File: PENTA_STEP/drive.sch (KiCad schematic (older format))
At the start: 17 parts, among them U3 TMC5160-TA

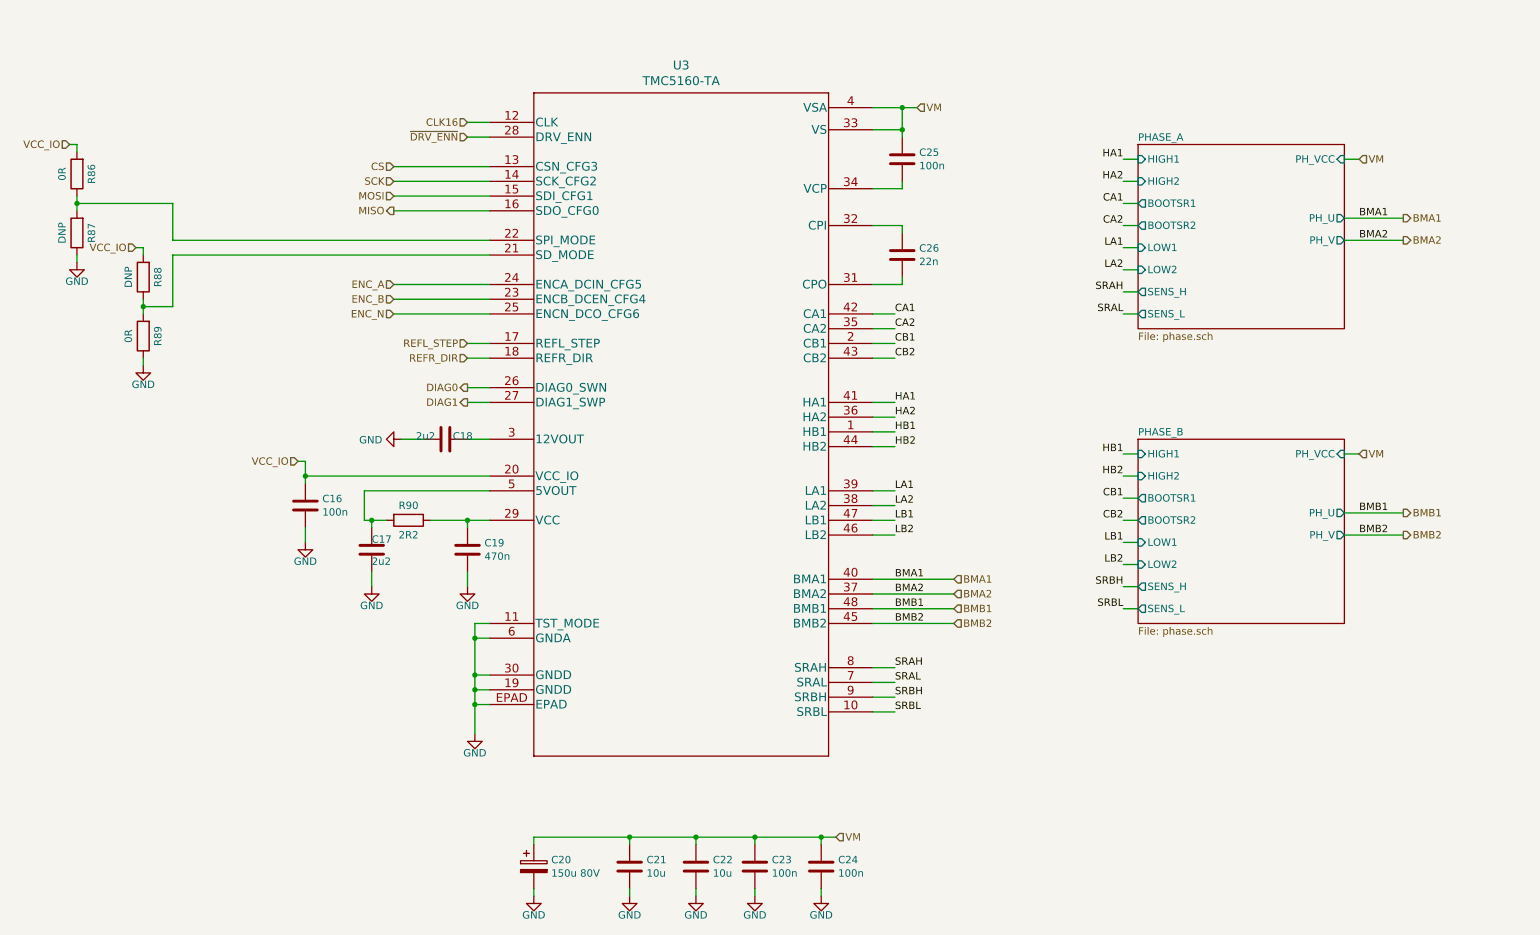
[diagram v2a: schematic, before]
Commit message: Added two FET-controlled outputs to the board
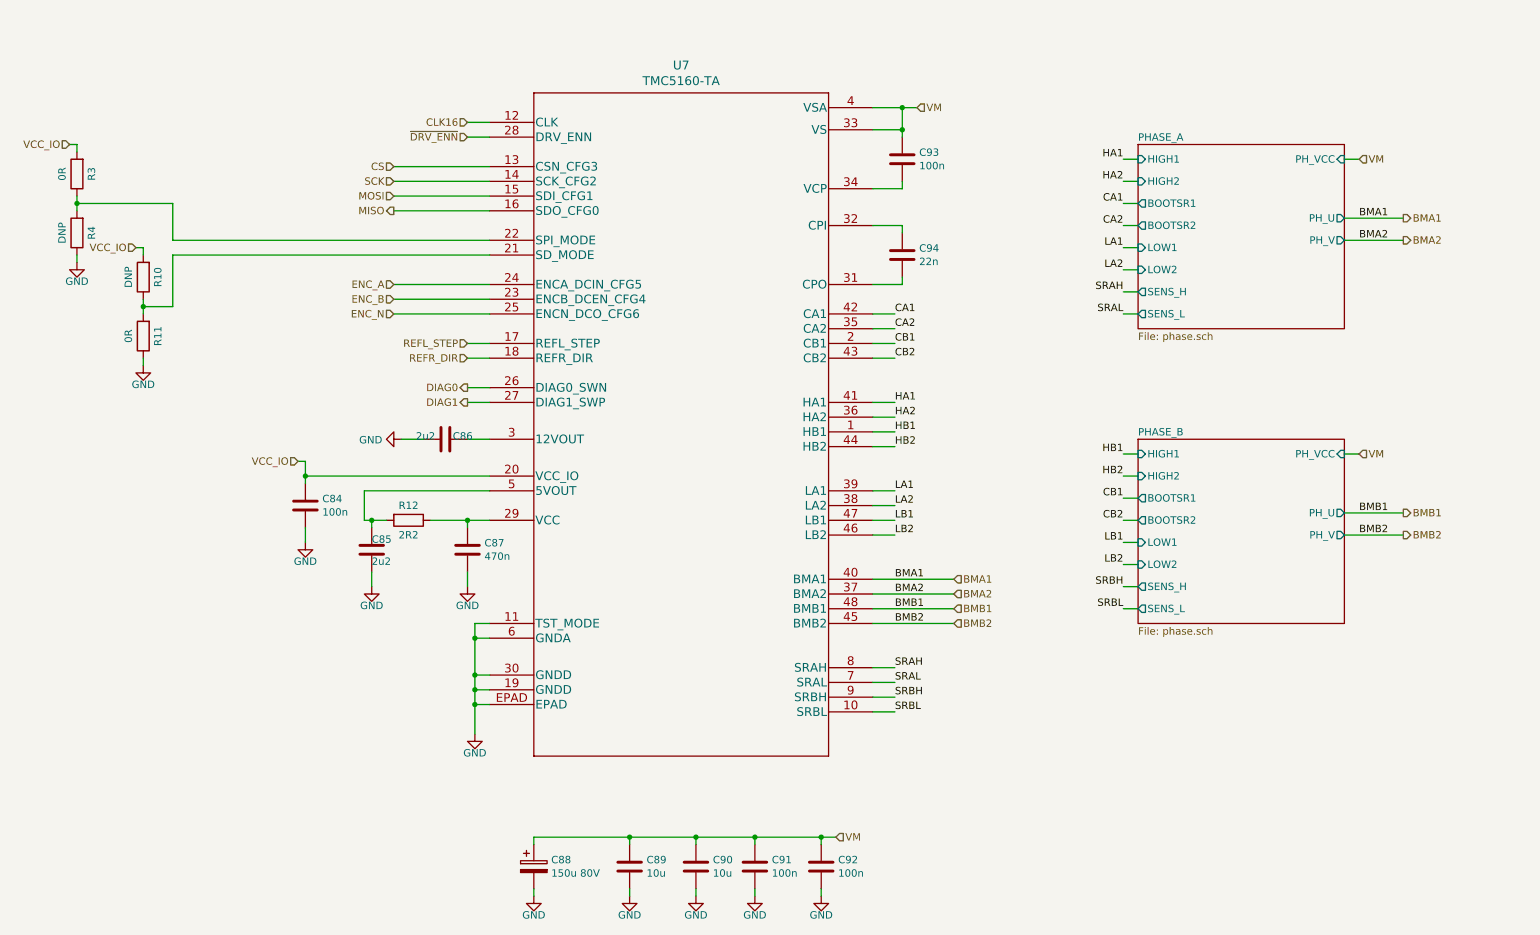
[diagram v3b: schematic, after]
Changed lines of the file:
@@
 $Descr A4 11693 8268
 encoding utf-8
-Sheet 2 16
+Sheet 14 16
 Title ""
 Date ""
@@
 AR Path="/5E50B60F/5E4B8E3D" Ref="U6"  Part="1"
 AR Path="/5F24B60D/5E4B8E3D" Ref="U7"  Part="1"
-F 0 "U3" H 5400 1737 60  0000 C CNN
+F 0 "U7" H 5400 1737 60  0000 C CNN
 F 1 "TMC5160-TA" H 5400 1631 60  0000 C CNN
 F 2 "CUSTOM_FP:TMC5160-TA" H 5400 1590 60  0001 C CNN
@@
 AR Path="/5E50B60F/5E4B8E77" Ref="C77"  Part="1"
 AR Path="/5F24B60D/5E4B8E77" Ref="C94"  Part="1"
-F 0 "C26" H 7015 2296 50  0000 L CNN
+F 0 "C94" H 7015 2296 50  0000 L CNN
 F 1 "22n" H 7015 2205 50  0000 L CNN
 F 2 "Capacitor_SMD:C_0603_1608Metric_Pad1.05x0.95mm_HandSolder" H 6938 2100 50  0001 C CNN
@@
 AR Path="/5E50B60F/5E4B8EAA" Ref="#PWR083"  Part="1"
 AR Path="/5F24B60D/5E4B8EAA" Ref="#PWR0101"  Part="1"
-F 0 "#PWR035" H 3500 3250 50  0001 C CNN
+F 0 "#PWR0101" H 3500 3250 50  0001 C CNN
 F 1 "GND" V 3505 3372 50  0000 R CNN
 F 2 "" H 3500 3500 50  0001 C CNN
@@
 AR Path="/5E50B60F/5E4B8EBB" Ref="C68"  Part="1"
 AR Path="/5F24B60D/5E4B8EBB" Ref="C85"  Part="1"
-F 0 "C17" H 3300 4150 50  0000 R BNN
+F 0 "C85" H 3300 4150 50  0000 R BNN
 F 1 "2u2" H 3300 4300 50  0000 R BNN
 F 2 "Capacitor_SMD:C_0603_1608Metric_Pad1.05x0.95mm_HandSolder" H 3338 4100 50  0001 C CNN
@@
 AR Path="/5E50B60F/5E4B8EC5" Ref="C67"  Part="1"
 AR Path="/5F24B60D/5E4B8EC5" Ref="C84"  Part="1"
-F 0 "C16" H 2965 3996 50  0000 L CNN
+F 0 "C84" H 2965 3996 50  0000 L CNN
 F 1 "100n" H 2965 3905 50  0000 L CNN
 F 2 "Capacitor_SMD:C_0603_1608Metric_Pad1.05x0.95mm_HandSolder" H 2888 3800 50  0001 C CNN
@@
 AR Path="/5E50B60F/5E4B8ECF" Ref="C70"  Part="1"
 AR Path="/5F24B60D/5E4B8ECF" Ref="C87"  Part="1"
-F 0 "C19" H 4065 4296 50  0000 L CNN
+F 0 "C87" H 4065 4296 50  0000 L CNN
 F 1 "470n" H 4065 4205 50  0000 L CNN
 F 2 "Capacitor_SMD:C_0603_1608Metric_Pad1.05x0.95mm_HandSolder" H 3988 4100 50  0001 C CNN
@@
 AR Path="/5E50B60F/5E4B8ED9" Ref="C76"  Part="1"
 AR Path="/5F24B60D/5E4B8ED9" Ref="C93"  Part="1"
-F 0 "C25" H 7015 1646 50  0000 L CNN
+F 0 "C93" H 7015 1646 50  0000 L CNN
 F 1 "100n" H 7015 1555 50  0000 L CNN
 F 2 "Capacitor_SMD:C_0603_1608Metric_Pad1.05x0.95mm_HandSolder" H 6938 1450 50  0001 C CNN
@@
 AR Path="/5E50B60F/5E4B8EEC" Ref="#PWR081"  Part="1"
 AR Path="/5F24B60D/5E4B8EEC" Ref="#PWR099"  Part="1"
-F 0 "#PWR033" H 2850 3950 50  0001 C CNN
+F 0 "#PWR099" H 2850 3950 50  0001 C CNN
 F 1 "GND" H 2850 4100 50  0000 C TNN
 F 2 "" H 2850 4200 50  0001 C CNN
@@
 AR Path="/5E50B60F/5E4B8EF7" Ref="R147"  Part="1"
 AR Path="/5F24B60D/5E4B8EF7" Ref="R12"  Part="1"
-F 0 "R90" V 3450 4050 50  0000 C CNN
+F 0 "R12" V 3450 4050 50  0000 C CNN
 F 1 "2R2" V 3650 4050 50  0000 C CNN
 F 2 "Resistor_SMD:R_0603_1608Metric_Pad1.05x0.95mm_HandSolder" V 3480 4050 50  0001 C CNN
@@
 AR Path="/5E50B60F/5E4B8F02" Ref="#PWR084"  Part="1"
 AR Path="/5F24B60D/5E4B8F02" Ref="#PWR0102"  Part="1"
-F 0 "#PWR036" H 3950 4250 50  0001 C CNN
+F 0 "#PWR0102" H 3950 4250 50  0001 C CNN
 F 1 "GND" H 3950 4400 50  0000 C TNN
 F 2 "" H 3950 4500 50  0001 C CNN
@@
 AR Path="/5E50B60F/5E4B8F08" Ref="#PWR082"  Part="1"
 AR Path="/5F24B60D/5E4B8F08" Ref="#PWR0100"  Part="1"
-F 0 "#PWR034" H 3300 4250 50  0001 C CNN
+F 0 "#PWR0100" H 3300 4250 50  0001 C CNN
 F 1 "GND" H 3300 4400 50  0000 C TNN
 F 2 "" H 3300 4500 50  0001 C CNN
@@
 AR Path="/5E50B60F/5E4B8F16" Ref="#PWR085"  Part="1"
 AR Path="/5F24B60D/5E4B8F16" Ref="#PWR0103"  Part="1"
-F 0 "#PWR037" H 4000 5250 50  0001 C CNN
+F 0 "#PWR0103" H 4000 5250 50  0001 C CNN
 F 1 "GND" H 4000 5400 50  0000 C TNN
 F 2 "" H 4000 5500 50  0001 C CNN
@@
 AR Path="/5E50B60F/5E4B8F3C" Ref="C71"  Part="1"
 AR Path="/5F24B60D/5E4B8F3C" Ref="C88"  Part="1"
-F 0 "C20" H 4518 6446 50  0000 L CNN
+F 0 "C88" H 4518 6446 50  0000 L CNN
 F 1 "150u 80V" H 4518 6355 50  0000 L CNN
 F 2 "CUSTOM_FP:CAPAE1350X1400N_EEVFK1J151Q" H 4438 6250 50  0001 C CNN
@@
 AR Path="/5E50B60F/5E4B8F46" Ref="C75"  Part="1"
 AR Path="/5F24B60D/5E4B8F46" Ref="C92"  Part="1"
-F 0 "C24" H 6465 6446 50  0000 L CNN
+F 0 "C92" H 6465 6446 50  0000 L CNN
 F 1 "100n" H 6465 6355 50  0000 L CNN
 F 2 "Capacitor_SMD:C_0603_1608Metric_Pad1.05x0.95mm_HandSolder" H 6388 6250 50  0001 C CNN
@@
 AR Path="/5E50B60F/5E4B8F50" Ref="C74"  Part="1"
 AR Path="/5F24B60D/5E4B8F50" Ref="C91"  Part="1"
-F 0 "C23" H 6015 6446 50  0000 L CNN
+F 0 "C91" H 6015 6446 50  0000 L CNN
 F 1 "100n" H 6015 6355 50  0000 L CNN
 F 2 "Capacitor_SMD:C_0603_1608Metric_Pad1.05x0.95mm_HandSolder" H 5938 6250 50  0001 C CNN
@@
 AR Path="/5E50B60F/5E4B8F5A" Ref="C72"  Part="1"
 AR Path="/5F24B60D/5E4B8F5A" Ref="C89"  Part="1"
-F 0 "C21" H 5165 6446 50  0000 L CNN
+F 0 "C89" H 5165 6446 50  0000 L CNN
 F 1 "10u" H 5165 6355 50  0000 L CNN
 F 2 "Capacitor_SMD:C_1210_3225Metric_Pad1.42x2.65mm_HandSolder" H 5088 6250 50  0001 C CNN
@@
 AR Path="/5E50B60F/5E4B8F64" Ref="C73"  Part="1"
 AR Path="/5F24B60D/5E4B8F64" Ref="C90"  Part="1"
-F 0 "C22" H 5615 6446 50  0000 L CNN
+F 0 "C90" H 5615 6446 50  0000 L CNN
 F 1 "10u" H 5615 6355 50  0000 L CNN
 F 2 "Capacitor_SMD:C_1210_3225Metric_Pad1.42x2.65mm_HandSolder" H 5538 6250 50  0001 C CNN
@@
 AR Path="/5E50B60F/5E4B8F88" Ref="#PWR086"  Part="1"
 AR Path="/5F24B60D/5E4B8F88" Ref="#PWR0104"  Part="1"
-F 0 "#PWR038" H 4400 6350 50  0001 C CNN
+F 0 "#PWR0104" H 4400 6350 50  0001 C CNN
 F 1 "GND" H 4400 6500 50  0000 C TNN
 F 2 "" H 4400 6600 50  0001 C CNN
@@
 AR Path="/5E50B60F/5E4B8F8E" Ref="#PWR087"  Part="1"
 AR Path="/5F24B60D/5E4B8F8E" Ref="#PWR0105"  Part="1"
-F 0 "#PWR039" H 5050 6350 50  0001 C CNN
+F 0 "#PWR0105" H 5050 6350 50  0001 C CNN
 F 1 "GND" H 5050 6500 50  0000 C TNN
 F 2 "" H 5050 6600 50  0001 C CNN
@@
 AR Path="/5E50B60F/5E4B8F94" Ref="#PWR088"  Part="1"
 AR Path="/5F24B60D/5E4B8F94" Ref="#PWR0106"  Part="1"
-F 0 "#PWR040" H 5500 6350 50  0001 C CNN
+F 0 "#PWR0106" H 5500 6350 50  0001 C CNN
 F 1 "GND" H 5500 6500 50  0000 C TNN
 F 2 "" H 5500 6600 50  0001 C CNN
@@
 AR Path="/5E50B60F/5E4B8F9A" Ref="#PWR089"  Part="1"
 AR Path="/5F24B60D/5E4B8F9A" Ref="#PWR0107"  Part="1"
-F 0 "#PWR041" H 5900 6350 50  0001 C CNN
+F 0 "#PWR0107" H 5900 6350 50  0001 C CNN
 F 1 "GND" H 5900 6500 50  0000 C TNN
 F 2 "" H 5900 6600 50  0001 C CNN
@@
 AR Path="/5E50B60F/5E4B8FA0" Ref="#PWR090"  Part="1"
 AR Path="/5F24B60D/5E4B8FA0" Ref="#PWR0108"  Part="1"
-F 0 "#PWR042" H 6350 6350 50  0001 C CNN
+F 0 "#PWR0108" H 6350 6350 50  0001 C CNN
 F 1 "GND" H 6350 6500 50  0000 C TNN
 F 2 "" H 6350 6600 50  0001 C CNN
@@
 AR Path="/5E50B60F/5E4B8FAE" Ref="R145"  Part="1"
 AR Path="/5F24B60D/5E4B8FAE" Ref="R10"  Part="1"
-F 0 "R88" V 1650 2400 50  0000 C CNN
+F 0 "R10" V 1650 2400 50  0000 C CNN
 F 1 "DNP" V 1850 2400 50  0000 C CNN
 F 2 "Resistor_SMD:R_0603_1608Metric_Pad1.05x0.95mm_HandSolder" V 1680 2400 50  0001 C CNN
@@
 AR Path="/5E50B60F/5E4B8FC3" Ref="R146"  Part="1"
 AR Path="/5F24B60D/5E4B8FC3" Ref="R11"  Part="1"
-F 0 "R89" V 1650 2800 50  0000 C CNN
+F 0 "R11" V 1650 2800 50  0000 C CNN
 F 1 "0R" V 1850 2800 50  0000 C CNN
 F 2 "Resistor_SMD:R_0603_1608Metric_Pad1.05x0.95mm_HandSolder" V 1680 2800 50  0001 C CNN
@@
 AR Path="/5E50B60F/5E4B8FD0" Ref="R143"  Part="1"
 AR Path="/5F24B60D/5E4B8FD0" Ref="R3"  Part="1"
-F 0 "R86" V 1200 1700 50  0000 C CNN
+F 0 "R3" V 1200 1700 50  0000 C CNN
 F 1 "0R" V 1400 1700 50  0000 C CNN
 F 2 "Resistor_SMD:R_0603_1608Metric_Pad1.05x0.95mm_HandSolder" V 1230 1700 50  0001 C CNN
@@
 AR Path="/5E50B60F/5E4B8FDA" Ref="R144"  Part="1"
 AR Path="/5F24B60D/5E4B8FDA" Ref="R4"  Part="1"
-F 0 "R87" V 1200 2100 50  0000 C CNN
+F 0 "R4" V 1200 2100 50  0000 C CNN
 F 1 "DNP" V 1400 2100 50  0000 C CNN
 F 2 "Resistor_SMD:R_0603_1608Metric_Pad1.05x0.95mm_HandSolder" V 1230 2100 50  0001 C CNN
@@
 AR Path="/5E50B60F/5E4B8FE1" Ref="#PWR080"  Part="1"
 AR Path="/5F24B60D/5E4B8FE1" Ref="#PWR098"  Part="1"
-F 0 "#PWR032" H 1750 2750 50  0001 C CNN
+F 0 "#PWR098" H 1750 2750 50  0001 C CNN
 F 1 "GND" H 1750 2900 50  0000 C TNN
 F 2 "" H 1750 3000 50  0001 C CNN
@@
 AR Path="/5E50B60F/5E4B8FE7" Ref="#PWR079"  Part="1"
 AR Path="/5F24B60D/5E4B8FE7" Ref="#PWR097"  Part="1"
-F 0 "#PWR031" H 1300 2050 50  0001 C CNN
+F 0 "#PWR097" H 1300 2050 50  0001 C CNN
 F 1 "GND" H 1300 2200 50  0000 C TNN
 F 2 "" H 1300 2300 50  0001 C CNN
@@
 AR Path="/5E50B60F/5E8C27DD" Ref="C69"  Part="1"
 AR Path="/5F24B60D/5E8C27DD" Ref="C86"  Part="1"
-F 0 "C18" V 3850 3450 50  0000 R BNN
+F 0 "C86" V 3850 3450 50  0000 R BNN
 F 1 "2u2" V 3850 3700 50  0000 R BNN
 F 2 "Capacitor_SMD:C_0603_1608Metric_Pad1.05x0.95mm_HandSolder" H 3838 3350 50  0001 C CNN

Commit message: majority routed, eliminated ATTINY coprocessor
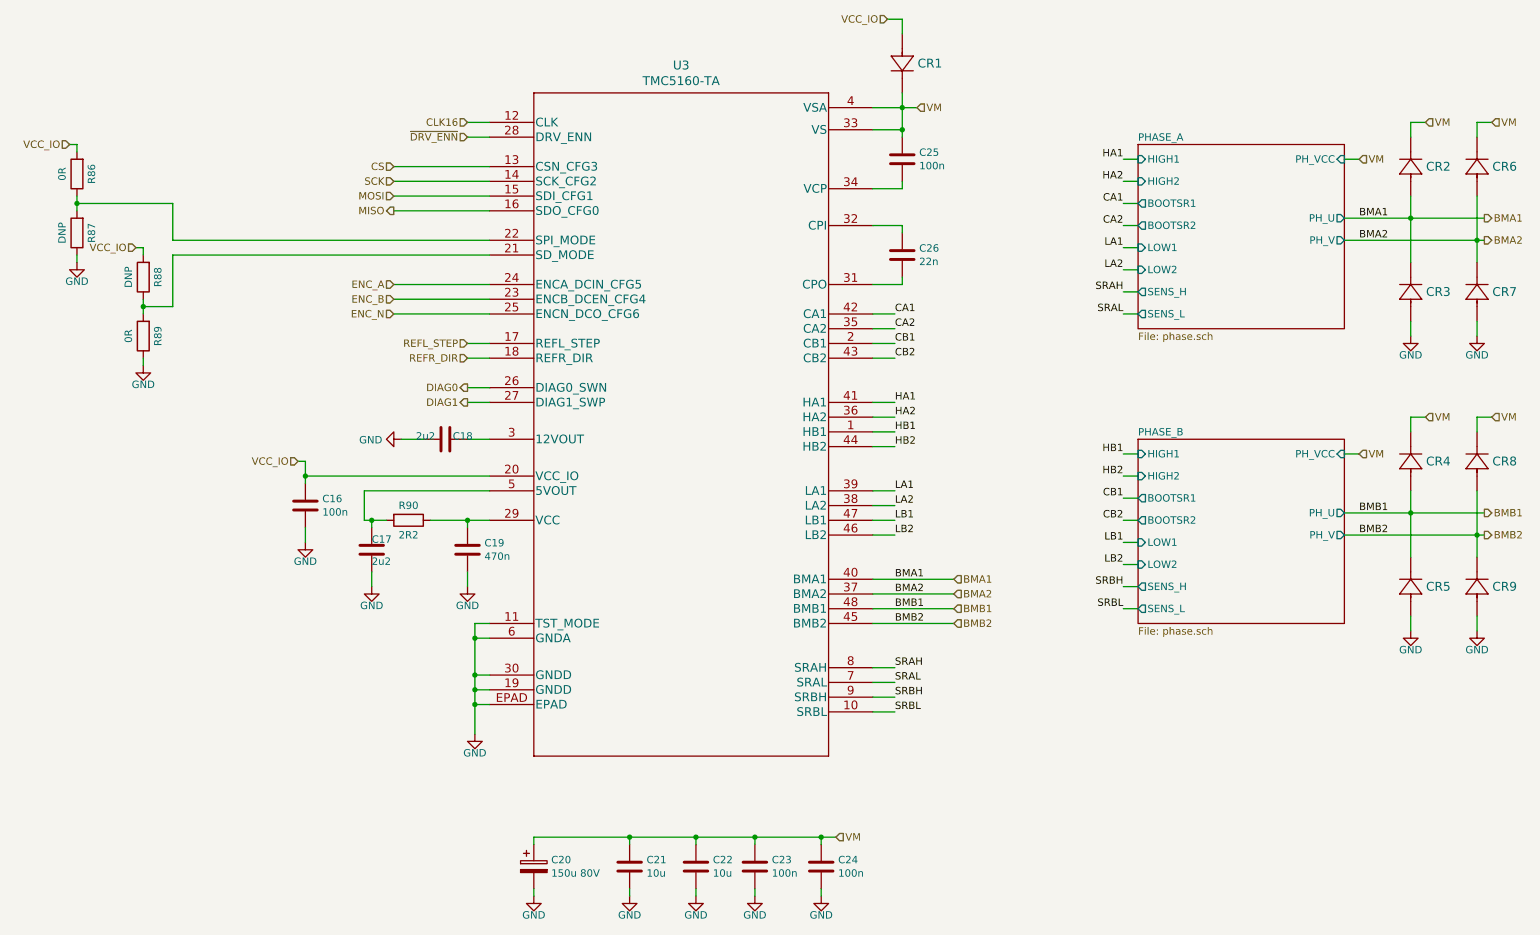
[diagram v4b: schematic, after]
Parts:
- added CR1, CR2, CR3, CR4, CR5, CR6, CR7, CR8, CR9: PMEG6010CEGWX, CUSTOM_FP:PMEG6010CEGWX, symbol CUSTOM:PMEG6010CEGWX
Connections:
- net BMA1: now also CR2.2, CR3.1
- net BMA2: now also CR6.2, CR7.1
- net BMB1: now also CR4.2, CR5.1
- net BMB2: now also CR8.2, CR9.1
- net GND: now also CR3.2, CR5.2, CR7.2, CR9.2
- net VCC_IO: now also CR1.2
- net VM: now also CR1.1, CR2.1, CR4.1, CR6.1, CR8.1

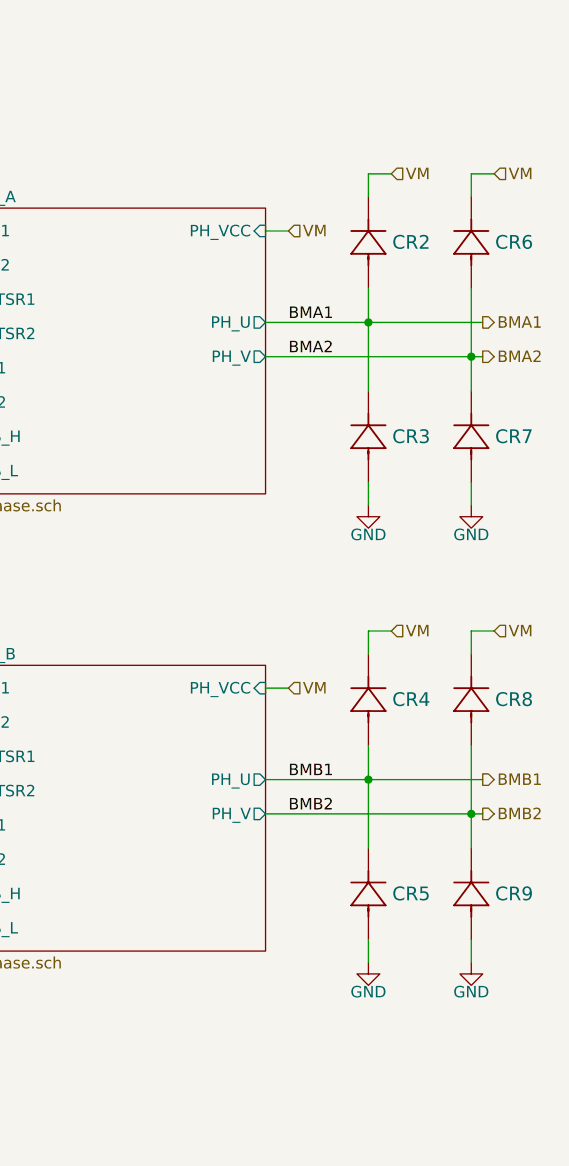
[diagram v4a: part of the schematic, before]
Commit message: completed preliminary routing, still need plane touchup
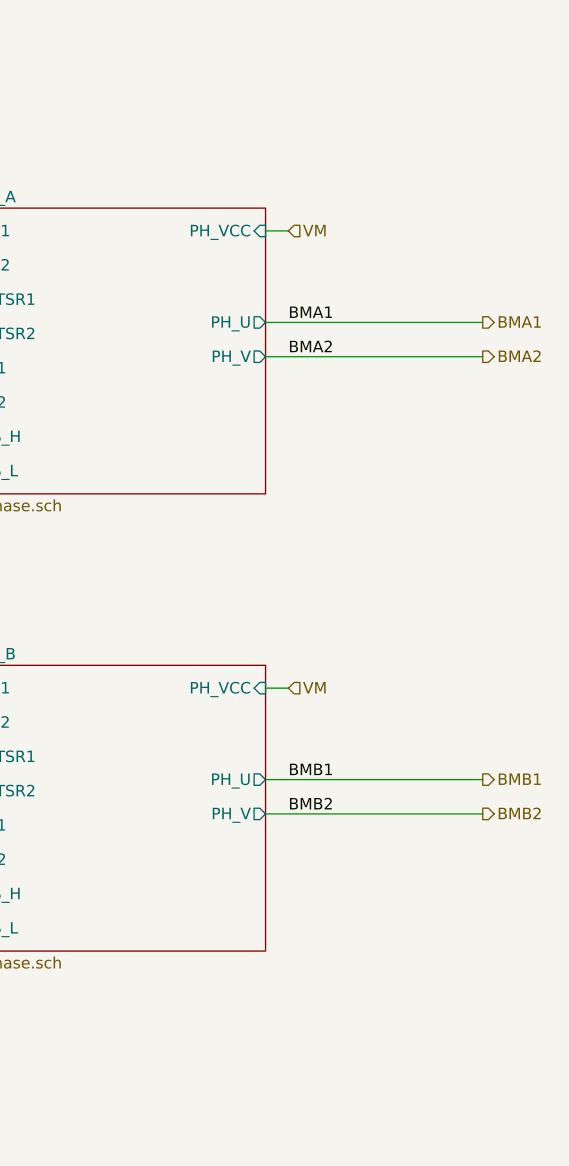
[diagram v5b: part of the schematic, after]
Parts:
- removed CR2, CR3, CR4, CR5, CR6, CR7, CR8, CR9: PMEG6010CEGWX, CUSTOM_FP:PMEG6010CEGWX, symbol CUSTOM:PMEG6010CEGWX
- CR1: DPN 1727-7339-1-ND -> S310FACT-ND; MPN PMEG6010CEGWX -> S310FA
